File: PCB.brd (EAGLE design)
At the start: 68.9 x 27.3 mm, 38 parts, among them IC1 MAX13448E, IC2 MAX13487E, IC3 LP2981A-50_DBV_5, IC4 TXB0101, IC5 TXB0101, IC6 SN74LVC2G04_DBV_6, IC7 MAX232E, IC8 SN74LVC1G11_DBV_6

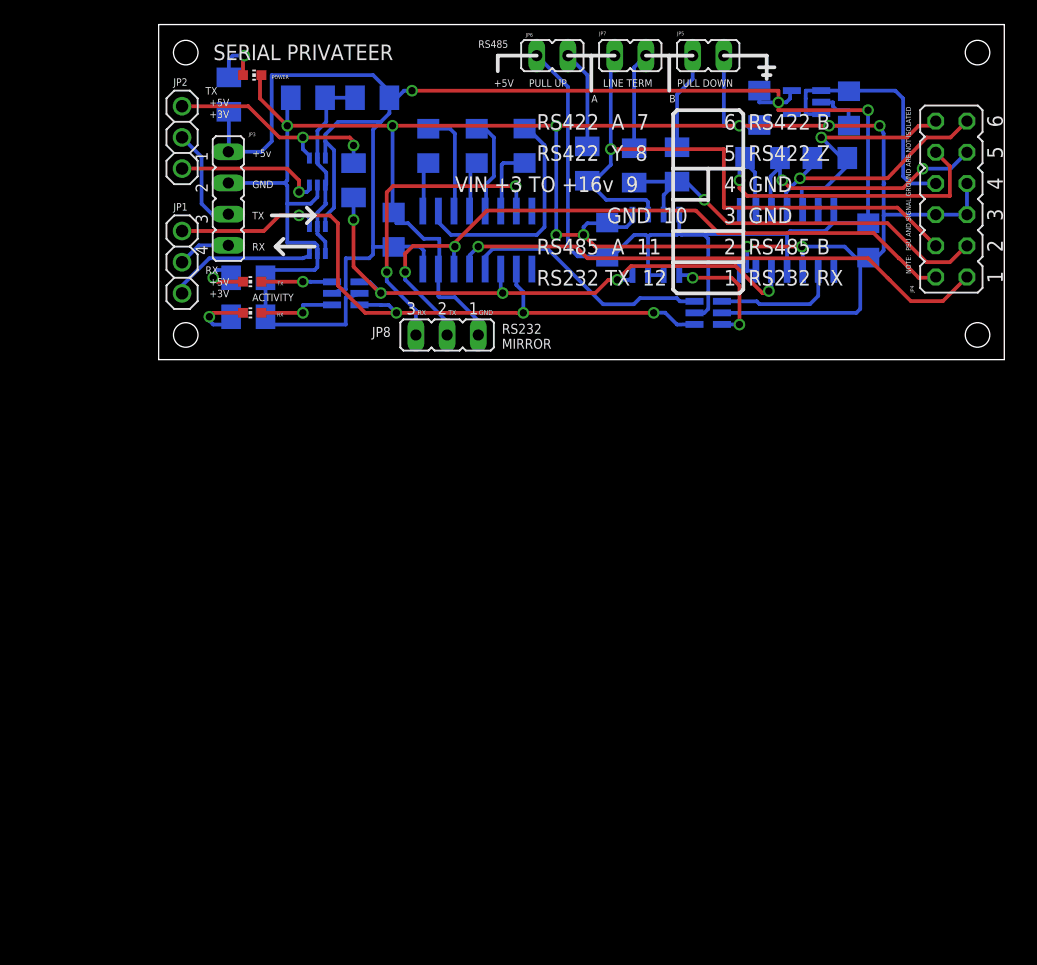
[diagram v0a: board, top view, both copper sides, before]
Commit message: Layout and silk screen tweaks
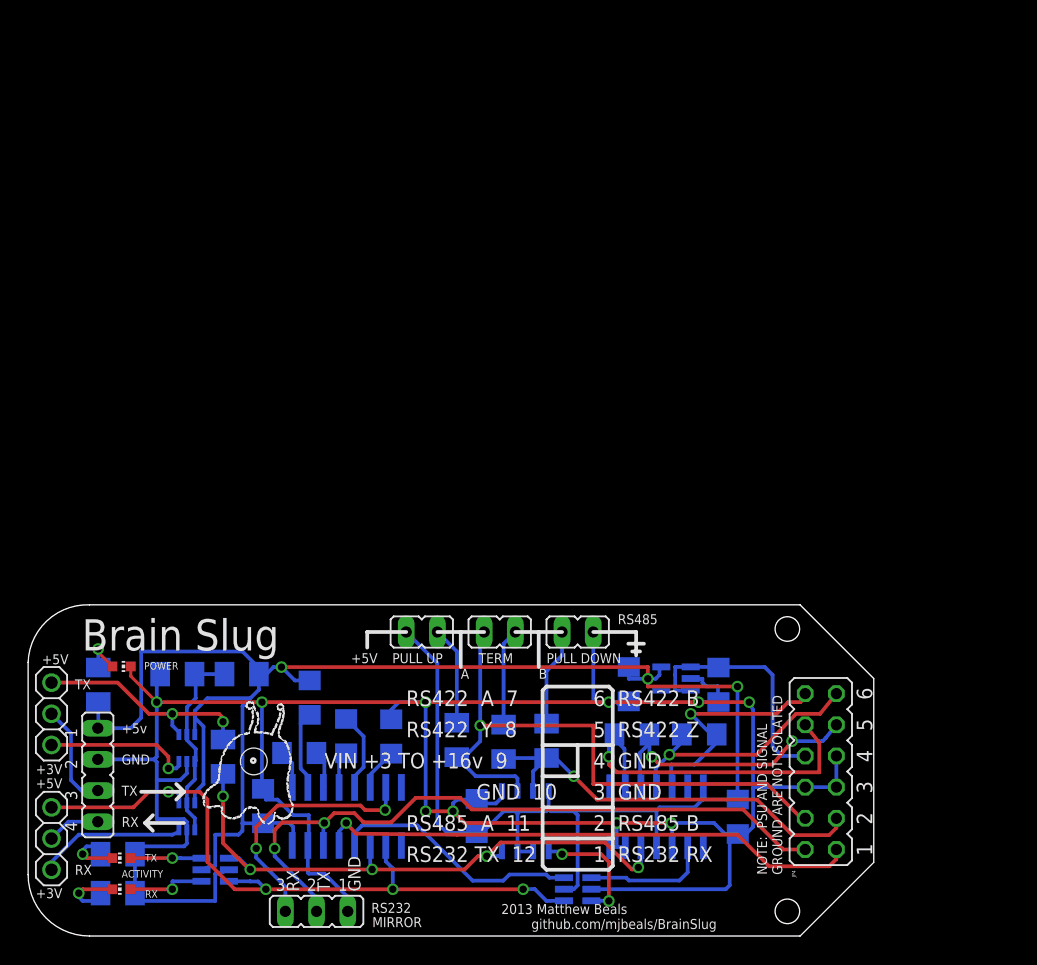
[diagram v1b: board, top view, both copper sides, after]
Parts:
- added C4: .1uF, adafruit:C1206
- C1, C2, C3: value (none) -> .1uF
- C10, C9: value (none) -> 2.2 uF
- C6: value (none) -> .1 uF
- R1, R3: value (none) -> 1440
- R10, R11, R8: value (none) -> 200
- R2, R4, R5: value (none) -> 120
- R6: value (none) -> 20k
- R7: value (none) -> 10k
- R9: value (none) -> 20
- moved C1 50.6 mm to (22.2, 14.9), turned to 0 degrees
- moved POWER 49.3 mm to (7.78, 22.0)
- moved C2 49.2 mm to (26.1, 16.3)
- moved R11 49.2 mm to (5.88, 20.5)
- moved C3 48.2 mm to (23.1, 19.5), turned to 90 degrees
- moved C10 48.1 mm to (49.1, 20.6)
- moved C5 48.1 mm to (19.3, 10.6)
- moved C6 48.1 mm to (36.7, 9.81)
- moved C7 48.1 mm to (58.0, 9.75)
- moved C9 48.1 mm to (56.4, 20.5)
- moved IC1 48.1 mm to (51.3, 9.75)
- moved IC2 48.1 mm to (40.7, 9.39)
- moved IC3 48.1 mm to (52.9, 21.0)
- moved IC4 48.1 mm to (13.1, 15.4)
- moved IC5 48.1 mm to (13.1, 9.78)
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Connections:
- net +5V: now also C3.2
- net GND: now also C4.2
- net RS232_VS-: now also C4.1; no longer C3.2
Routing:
- net RS232_VS+: track 19.1 -> 6.46 mm
- net RS232_C1-: track 8.68 -> 3.84 mm
- net RS232_RX_MIRROR: track 25.4 -> 21.1 mm
- net GND: track 216.4 -> 218.9 mm
- net RS232_VS-: track 5.73 -> 3.46 mm
- net +5V: track 178.9 -> 180.5 mm
- net RS232_C2-: track 7.98 -> 6.47 mm
- net RS232_C2+: track 4.36 -> 3.02 mm
- net N$2: track 4.49 -> 3.42 mm
- net RS232_C1+: track 4.09 -> 3.15 mm
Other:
- board size 68.9 x 27.3 mm -> 68.9 x 27 mm
- board text added: "2013 Matthew Beals"
- board text added: "Brain Slug"
- board text added: "GROUND ARE NOT ISOLATED"
- board text added: "MIRROR"
- board text added: "NOTE: PSU AND SIGNAL"
- board text added: "RS232"
- board text added: "TERM"
- board text added: "github.com/mjbeals/BrainSlug"
- board text removed: "LINE TERM"
- board text removed: "NOTE: PSU AND SIGNAL GROUND ARE NOT ISOLATED"
- board text removed: "RS232 MIRROR"
- board text removed: "SERIAL PRIVATEER"

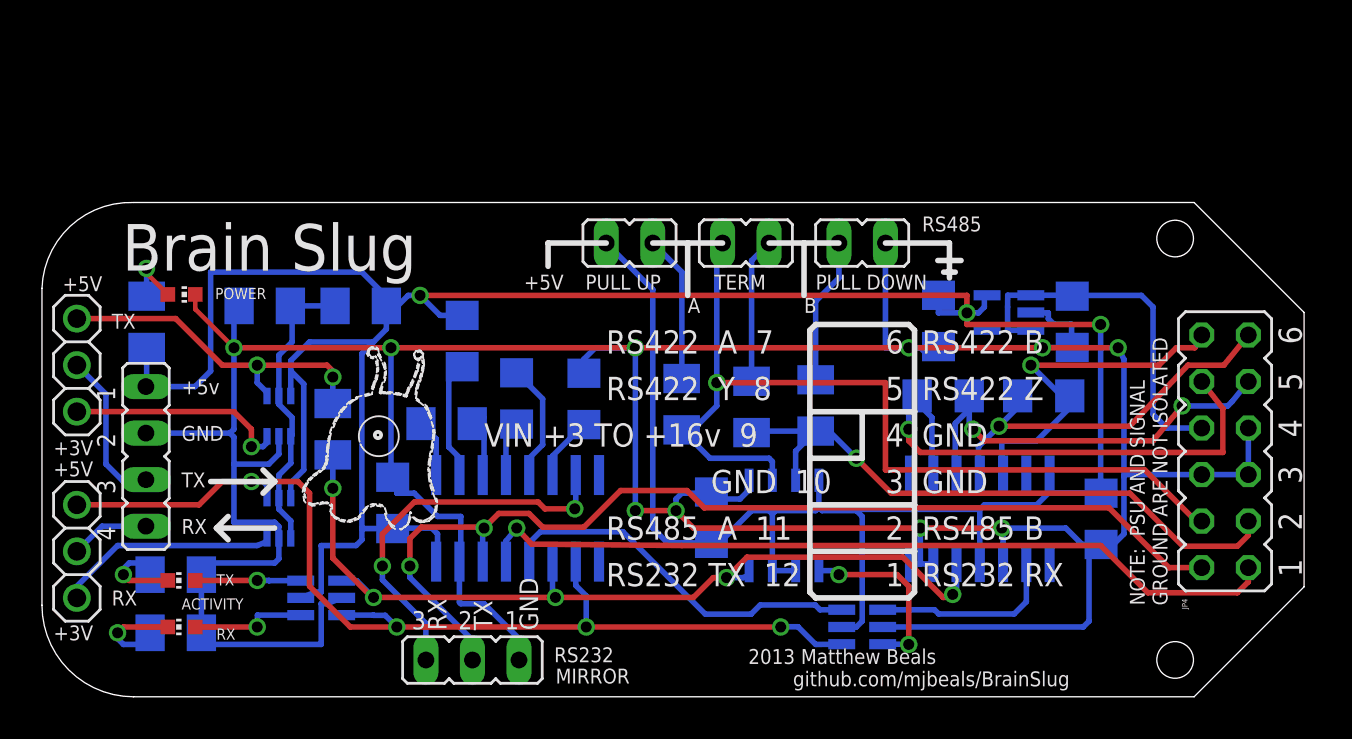
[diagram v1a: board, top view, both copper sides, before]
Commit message: REV 1.2
Added onboard USB and supply isolation
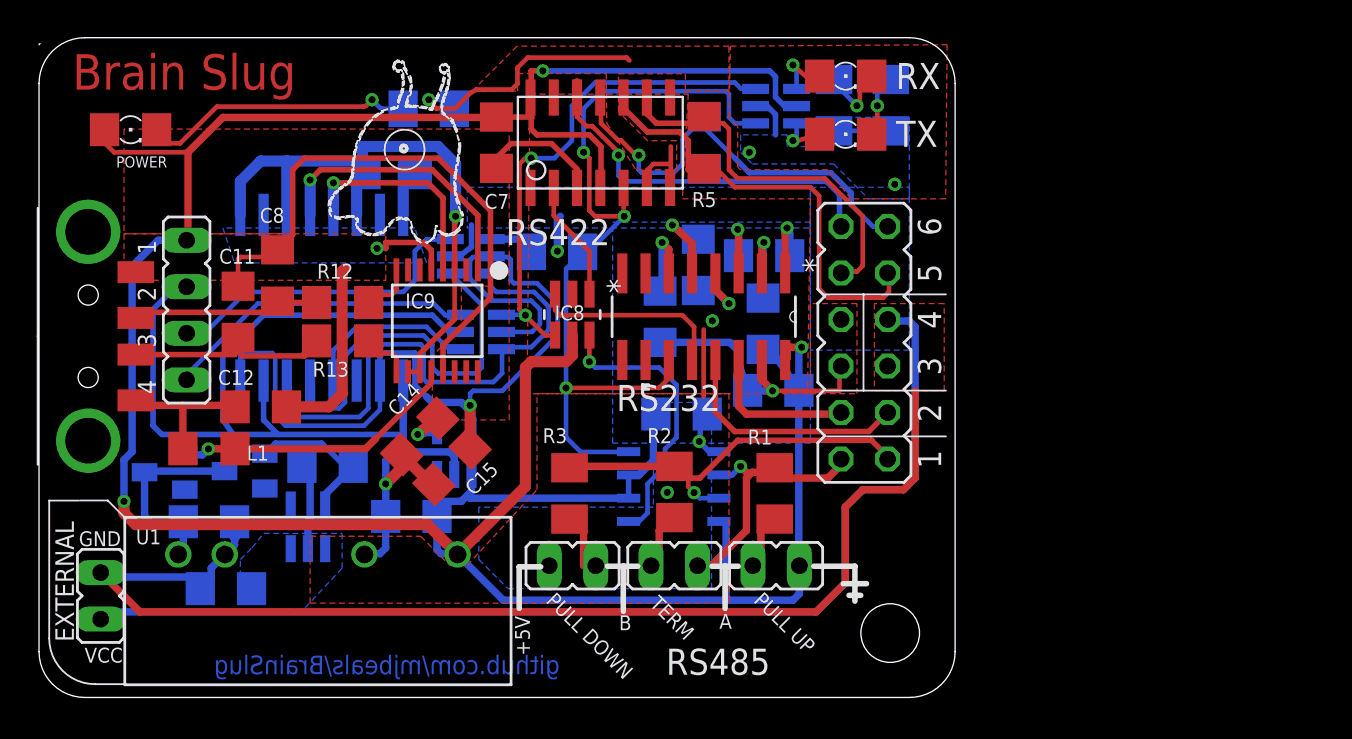
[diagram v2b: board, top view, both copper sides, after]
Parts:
- removed C10: 2.2 uF, adafruit:C1206
- removed IC4, IC5: TXB0101, TI:DCK
- removed JP2: (no value), adafruit:1X03
- removed JP8: (no value), jumper:JP2
- removed R11: 200, adafruit:M1206
- removed R7: 10k, adafruit:M1206
- added C11, C12, C13, C16, C17, C18, C8: .1uF, adafruit:C1206
- added C14: .01 uF, adafruit:C1206
- added C15: 2.2 uF, adafruit:C1206
- added D1, D6: (no value), dp_devices:SOT-23
- added IC9: IC_FT230X-SSOP-16, dp_devices:SSOP-16-FTDI
- added L1: (no value), dp_devices:FB1206
- added R12, R13: 27R, adafruit:R1206
- added U$1, U$2: TS5A3159-Q1, TI:DBV6
- added U1: DCH010505S_EDJ_4, TI:EDJ4
- added U3: REG101-3_DBV_5, TI:DBV5
- added U5: ISO7231C_DW_16, TI:DW16
- added X1: USB-A, adafruit:MOLEX_480371000
- C5: value (none) -> .1uF
- C7: value (none) -> .1 uF
- JP1: device adafruit:1X03 -> jumper:JP1
- POWER, RX, TX: device adafruit:CHIP-LED0603 -> adafruit:1206
- R6: value 20k -> 200
- moved C9 48.4 mm to (10.2, 5.94), turned to 0 degrees
- moved RX 47.1 mm to (44.0, 33.9), turned to 0 degrees
- moved R10 46.7 mm to (46.5, 32.3), turned to 90 degrees
- moved R8 46.0 mm to (43.4, 32.3), turned to 90 degrees
- moved TX 43.7 mm to (44.0, 30.7), turned to 0 degrees
- moved IC3 40.0 mm to (14.7, 9.32), turned to 90 degrees
- moved C7 38.9 mm to (25.0, 30.3), flipped to the top
- moved IC6 36.6 mm to (40.2, 32.3), turned to 180 degrees
- moved IC1 29.2 mm to (30.6, 30.3), flipped to the top
- moved JP5 23.7 mm to (29.1, 7.19), turned to 90 degrees
- moved IC8 23.3 mm to (29.1, 20.9), flipped to the top, turned to 270 degrees
- moved R4 23.1 mm to (36.3, 30.3), turned to 90 degrees
- moved C5 21.7 mm to (40.1, 16.8), turned to 0 degrees
- moved JP4 20.6 mm to (45.0, 19.4)
- moved C1 19.6 mm to (39.6, 24.1), turned to 180 degrees
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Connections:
- removed net N$2: POWER.A, R11.1
- removed net RS232_RX_MIRROR: IC7.7, JP8.3
- removed net RX: JP1.2, JP3.4
- removed net TX: JP2.2, JP3.3
- removed net UART_RX3V: IC5.P3, JP1.3
- removed net UART_TX3V: IC4.P3, JP2.3
- removed net UART_TXLOAD: IC4.P4, JP2.1, R9.2
- removed net VUNREG: C9.1, IC3.1, IC3.3, JP4.8
- new net BT_RX: JP3.4, U$1.3
- new net BT_TX: JP3.3, U$2.3
- new net EXT_5V: C18.1, D6.1, IC3.5
- new net EXT_GND: C16.2, C18.2, C9.2, IC3.2, JP1.2, JP4.5, U1.2
- new net EXT_VCC: C9.1, IC3.1, IC3.3, JP1.1, JP4.7
- new net N$10: C11.2, R13.1, X1.2
- new net N$11: C14.1, U3.4
- new net N$4: IC9.1, U5.4
- new net N$5: IC9.4, U5.5
- new net N$6: POWER.C, R6.2
- new net N$7: IC9.9, R13.2
- new net N$8: IC9.8, R12.2
- new net N$9: C8.2, R12.1, X1.3
- new net UART_TX_1: R9.2, U$2.4
- new net USB_3V: C13.1, IC9.10, IC9.11, IC9.3, U5.1, U5.3, U5.6
- new net USB_5V: D1.1, IC9.12, L1.2
- new net USB_GND: C11.1, C12.1, C13.2, C8.1, IC9.13, IC9.5, U5.2, U5.8, X1.4
- new net USB_RX: U$1.1, U5.12
- new net USB_SWITCH: U$1.6, U$2.6, U5.14
- new net USB_TX: U$2.1, U5.13
- new net USB_VCC: C16.1, D1.3, D6.3, U1.1
- new net VCC_USB: C12.2, L1.1, X1.1
- net +3V: now also C15.1, U$1.5, U$2.5, U3.5, U5.10, U5.16; no longer IC4.P1, IC4.P5, IC5.P1, IC5.P5, R6.1, R7.2
- net +5V: now also C17.1, POWER.A, U1.4, U3.1, U3.3; no longer C10.1, IC3.5, IC4.P6, IC5.P6, R11.2, R7.1
- net GND: now also C14.2, C15.2, C17.2, JP4.8, R6.1, U$1.2, U$2.2, U1.3, U3.2, U5.15, U5.9; no longer C10.2, C9.2, IC3.2, IC4.P2, IC5.P2, JP4.5, JP4.7, JP8.1, POWER.C, R6.2
- net RS232_RO: now also IC8.3; no longer IC8.6
- net RS232_RX: now also JP4.3; no longer JP4.1
- net RS232_TX: now also JP4.4; no longer JP4.2, JP8.2
- net RS485_A: now also JP4.2; no longer JP4.4
- net RS485_B: now also JP4.1; no longer JP4.3
- net RS485_RO: now also IC8.6; no longer IC8.3
- net UART_RX: now also U$1.4; no longer IC5.P4, IC7.10, JP1.1
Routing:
- net GND: track 218.9 -> 123.4 mm, vias 10 -> 9
- net EXT_GND: track 0.00 -> 75.0 mm
- net EXT_VCC: track 0.00 -> 59.7 mm
- net USB_GND: track 0.00 -> 49.9 mm, vias 0 -> 1
- net RS232_TX: track 56.9 -> 8.33 mm, vias 2 -> 0
- net RS485_A: track 50.6 -> 15.0 mm
- net USB_3V: track 0.00 -> 34.5 mm, vias 0 -> 1
- net +3V: track 16.3 -> 50.6 mm, vias 0 -> 1
- net RS232_RX: track 44.4 -> 13.1 mm, vias 1 -> 0
- net UART_RX: track 57.6 -> 27.8 mm, vias 4 -> 2
- net USB_SWITCH: track 0.00 -> 29.6 mm
- net VUNREG: track 21.4 -> 0.00 mm
- net USB_TX: track 0.00 -> 21.4 mm
- net RS232_RX_MIRROR: track 21.1 -> 0.00 mm, vias 2 -> 0
- net UART_TXLOAD: track 18.6 -> 0.00 mm, vias 2 -> 0
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- added copper zone on layer 1, net EXT_GND
- added copper zone on layer 16, net EXT_VCC
- added copper zone on layer 1, net GND
- added copper zone on layer 16, net GND
- added copper zone on layer 1, net USB_GND
- added copper zone on layer 16, net USB_GND
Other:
- board size 68.9 x 27 mm -> 50 x 36 mm
- board text added: "1"
- board text added: "2"
- board text added: "3"
- board text added: "4"
- board text added: "5"
- board text added: "6"
- board text added: "EXTERNAL"
- board text added: "RS232 RX"
- board text added: "RS232 TX"
- board text added: "RS422"
- board text added: "RS422 A"
- board text added: "RS422 B"
- board text added: "RS422 Y"
- board text added: "RS422 Z"
- board text added: "RS485 A"
- board text added: "RS485 B"
- board text added: "SIGNAL GND"
- board text added: "VCC"
- board text added: "Vcc +3 TO +16v"
- board text added: "Vss GND"
- board text removed: "+3V"
- board text removed: "1 RS232 RX"
- board text removed: "2 RS485 B"
- board text removed: "2013 Matthew Beals"
- board text removed: "3 GND"
- board text removed: "4 GND"
- board text removed: "5 RS422 Z"
- board text removed: "6 RS422 B"
- board text removed: "ACTIVITY"
- board text removed: "GND 10"
- board text removed: "GROUND ARE NOT ISOLATED"
- board text removed: "MIRROR"
- board text removed: "NOTE: PSU AND SIGNAL"
- board text removed: "RS232 TX 12"
- board text removed: "RS422 A 7"
- board text removed: "RS422 Y 8"
- board text removed: "RS485 A 11"
- board text removed: "VIN +3 TO +16v 9"

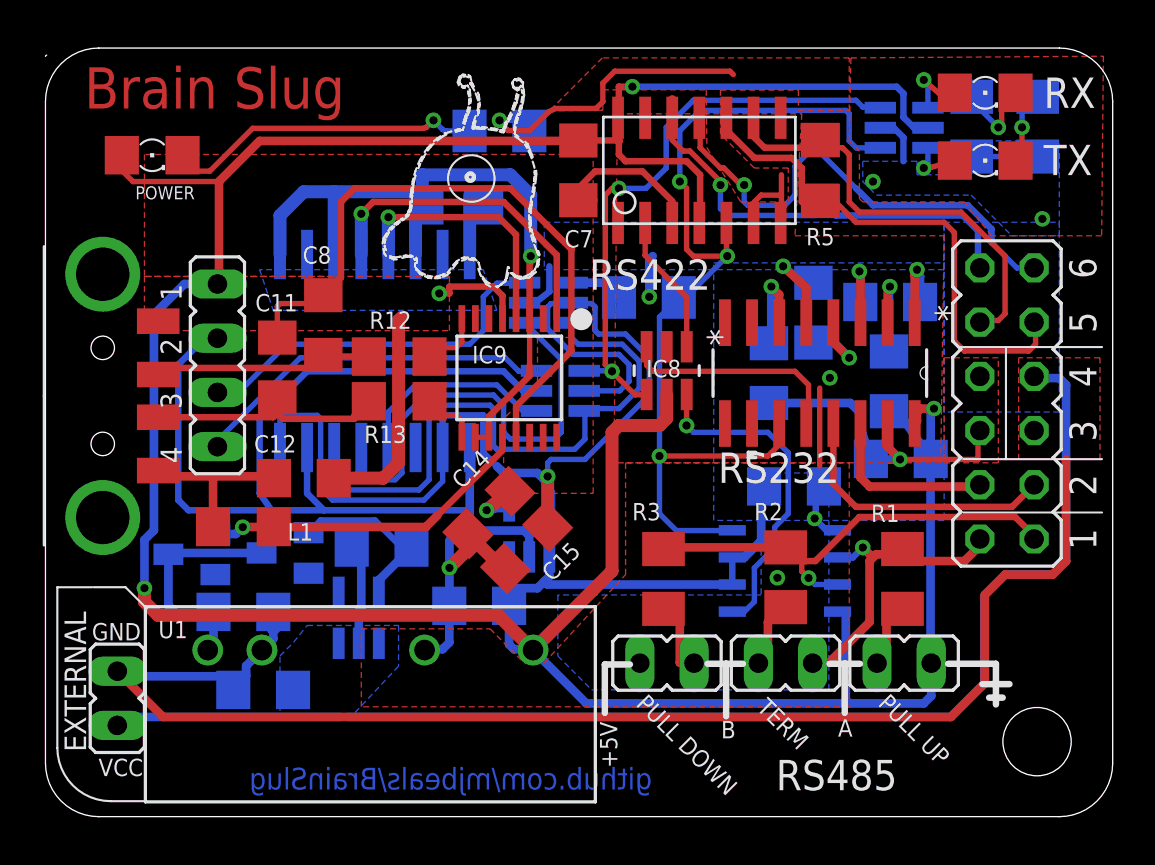
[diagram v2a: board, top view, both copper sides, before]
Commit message: updates to document V1rA Eratta
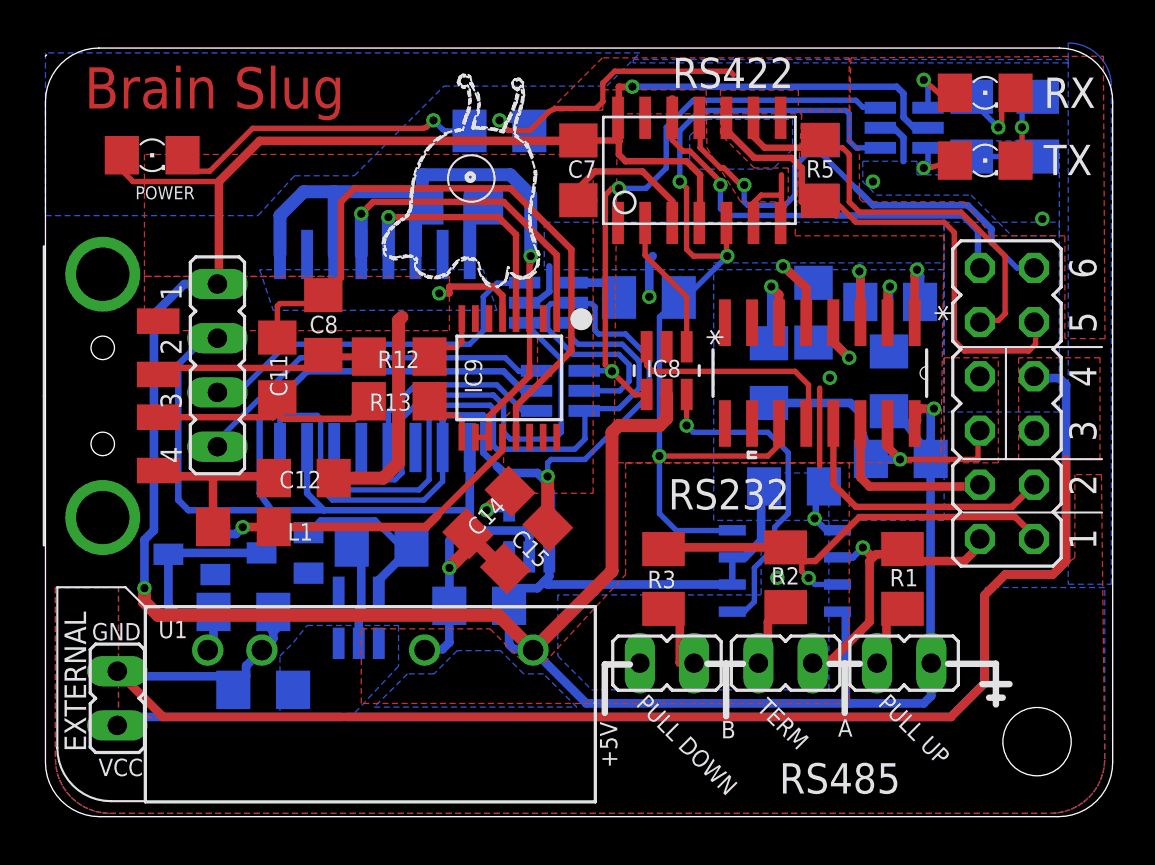
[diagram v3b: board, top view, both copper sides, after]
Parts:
- C11, C8: value .1uF -> 47pF
- C12: value .1uF -> .01uF
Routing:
- added copper zone on layer 16, net N$12
- added copper zone on layer 16, net N$13
- added copper zone on layer 16, net N$14
- added copper zone on layer 16, net N$15
- added copper zone on layer 1, net N$2
- added copper zone on layer 16, net N$2
- added copper zone on layer 16, net N$3
